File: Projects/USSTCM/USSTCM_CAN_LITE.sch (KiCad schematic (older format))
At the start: 1 part, among them U2 MCP25625

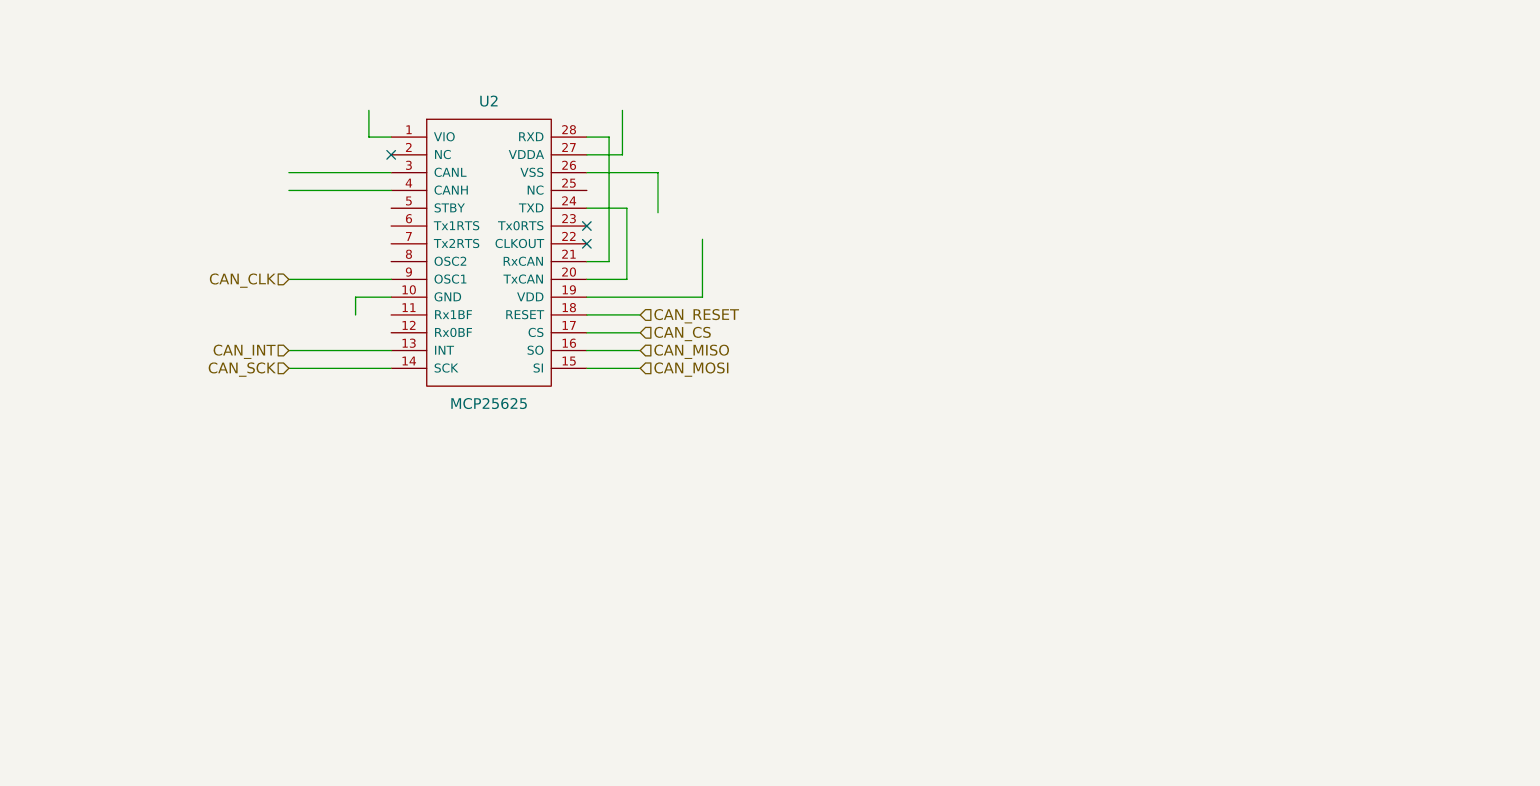
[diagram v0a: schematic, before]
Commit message: More organization of CMIO board
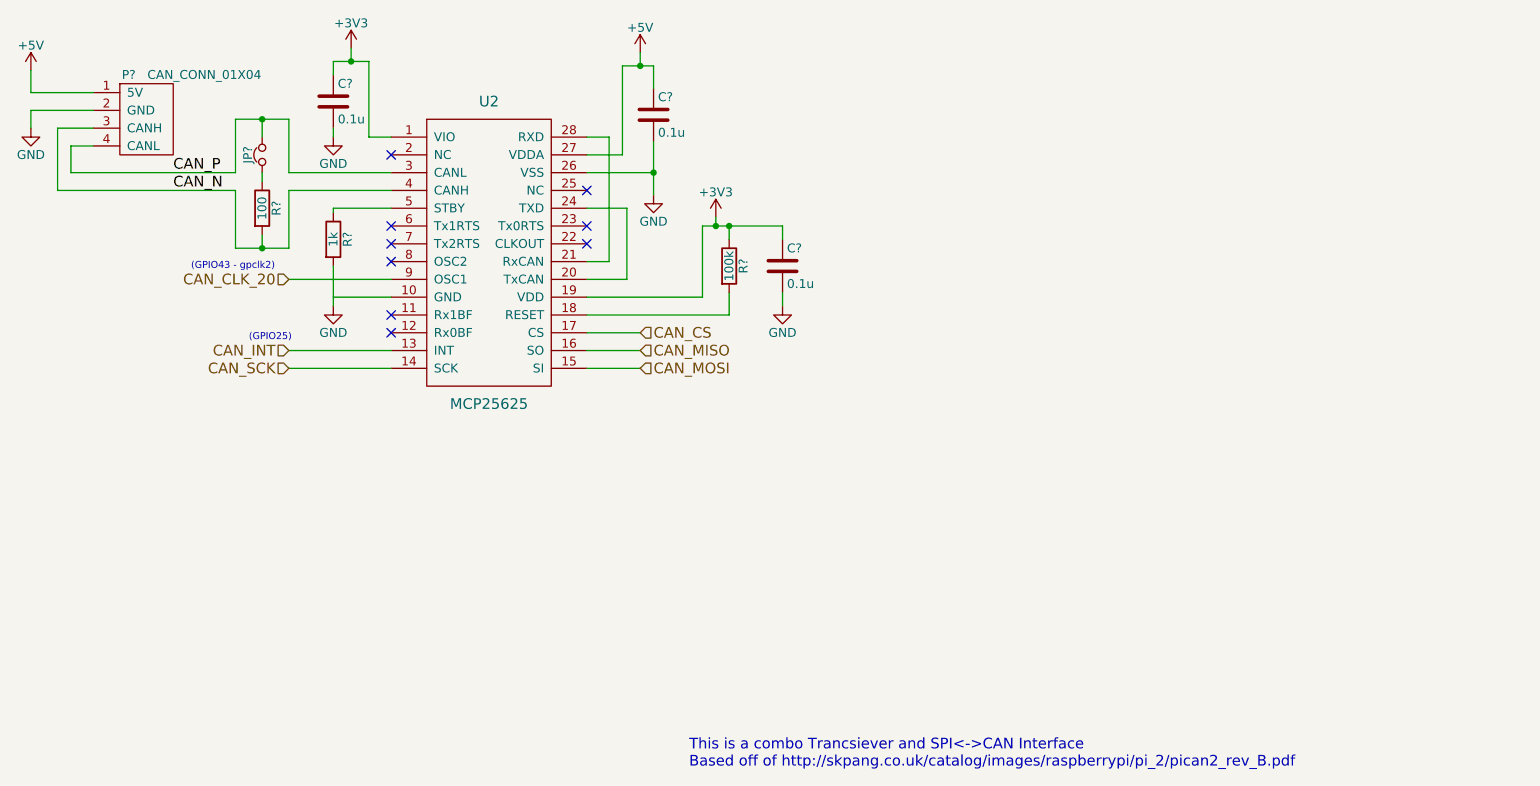
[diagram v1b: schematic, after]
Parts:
- added C? (x3): 0.1u, symbol C
- added JP?: Jumper_NC_Small, symbol Jumper_NC_Small
- added P?: CAN_CONN_01X04, symbol CAN_CONN_01X04
- added R?: 100, symbol R
- added R?: 100k, symbol R
- added R?: 1k, symbol R
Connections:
- net labels added: +3V3, +5V, CAN_CLK_20, CAN_N, CAN_P, GND
- net labels removed: CAN_CLK, CAN_RESET
- wire segments 25 -> 59
- no-connect marks 3 -> 9
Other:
- note added: "(GPIO25)"
- note added: "(GPIO43 - gpclk2)"
- note added: "This is a combo Trancsiever and SPI<->CAN Interface\nBased off of http://skpang.co.uk/catalog/images/raspberrypi/pi_2/pican2_rev_B.pdf"

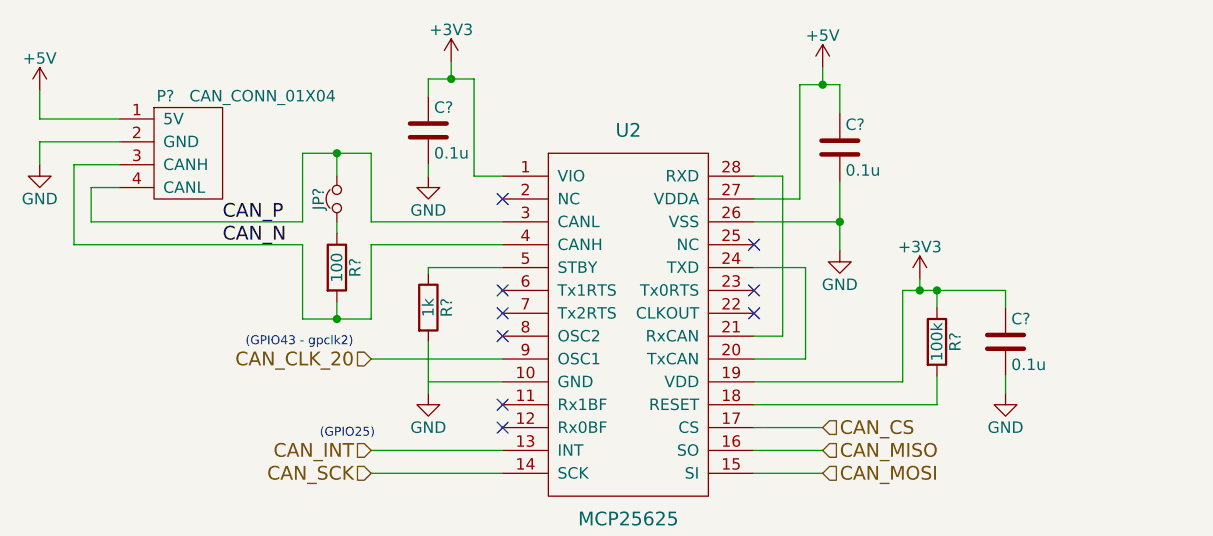
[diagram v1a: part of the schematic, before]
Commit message: added differential routes
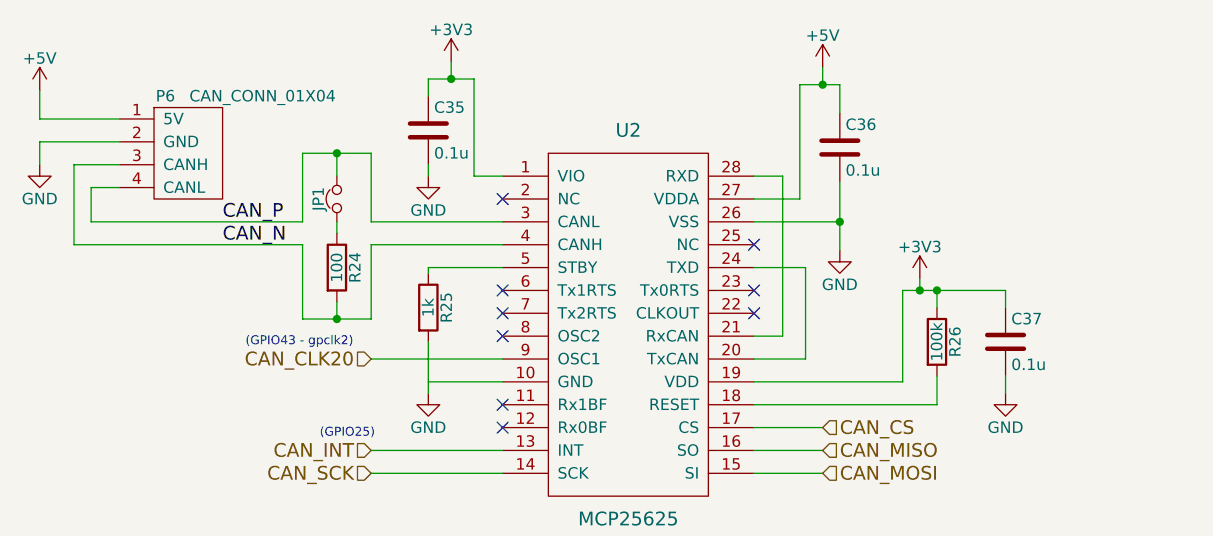
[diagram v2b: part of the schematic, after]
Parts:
- C35, C36, C37: renamed from C?; footprint (none) -> Capacitors_SMD:C_0805
- JP1: renamed from JP?; footprint (none) -> USST-footprints:J_0603
- P6: renamed from P?; footprint (none) -> Pin_Headers:Pin_Header_Angled_1x04_Pitch2.54mm
- R24, R25, R26: renamed from R?; footprint (none) -> Resistors_SMD:R_0805
- U2: footprint (none) -> Housings_SSOP:SSOP-28_5.3x10.2mm_Pitch0.65mm
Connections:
- net CAN_CLK_20 renamed CAN_CLK20
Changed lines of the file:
@@
 $Descr A4 11693 8268
 encoding utf-8
-Sheet 4 7
+Sheet 4 8
 Title ""
 Date ""
@@
 F 0 "U2" H 5825 4450 60  0000 C CNN
 F 1 "MCP25625" H 5825 2750 60  0000 C CNN
-F 2 "" H 5825 4000 60  0001 C CNN
+F 2 "Housings_SSOP:SSOP-28_5.3x10.2mm_Pitch0.65mm" H 5825 4000 60  0001 C CNN
 F 3 "" H 5825 4000 60  0001 C CNN
 	1    5825 3550
@@
 NoConn ~ 5275 2950
 Text HLabel 4700 3650 0    60   Input ~ 0
-CAN_CLK_20
+CAN_CLK20
 Text HLabel 4700 4050 0    60   Input ~ 0
 CAN_INT
@@
 NoConn ~ 6375 3450
 $Comp
-L GND #PWR?
+L GND #PWR076
 U 1 1 58E357D9
 P 4950 3800
-F 0 "#PWR?" H 4950 3550 50  0001 C CNN
+F 0 "#PWR076" H 4950 3550 50  0001 C CNN
 F 1 "GND" H 4950 3650 50  0000 C CNN
 F 2 "" H 4950 3800 50  0000 C CNN
@@
 (GPIO25)
 $Comp
-L R R?
+L R R24
 U 1 1 58E363A9
 P 4550 3250
-F 0 "R?" V 4630 3250 50  0000 C CNN
+F 0 "R24" V 4630 3250 50  0000 C CNN
 F 1 "100" V 4550 3250 50  0000 C CNN
-F 2 "" V 4480 3250 50  0000 C CNN
+F 2 "Resistors_SMD:R_0805" V 4480 3250 50  0001 C CNN
 F 3 "" H 4550 3250 50  0000 C CNN
 	1    4550 3250
@@
 $EndComp
 $Comp
-L Jumper_NC_Small JP?
+L Jumper_NC_Small JP1
 U 1 1 58E36400
 P 4550 2950
-F 0 "JP?" H 4550 3030 50  0000 C CNN
+F 0 "JP1" H 4550 3030 50  0000 C CNN
 F 1 "Jumper_NC_Small" H 4560 2890 50  0001 C CNN
-F 2 "" H 4550 2950 50  0000 C CNN
+F 2 "USST-footprints:J_0603" H 4550 2950 50  0001 C CNN
 F 3 "" H 4550 2950 50  0000 C CNN
 	1    4550 2950
@@
 $EndComp
 $Comp
-L CAN_CONN_01X04 P?
+L CAN_CONN_01X04 P6
 U 1 1 58E36E81
 P 3800 2750
-F 0 "P?" H 3800 3000 50  0000 C CNN
+F 0 "P6" H 3800 3000 50  0000 C CNN
 F 1 "CAN_CONN_01X04" H 4225 3000 50  0000 C CNN
-F 2 "" H 3800 2750 50  0000 C CNN
+F 2 "Pin_Headers:Pin_Header_Angled_1x04_Pitch2.54mm" H 3800 2750 50  0001 C CNN
 F 3 "" H 3800 2750 50  0000 C CNN
 	1    3800 2750
@@
 $EndComp
 $Comp
-L +5V #PWR?
+L +5V #PWR077
 U 1 1 58E38EE5
 P 3250 2475
-F 0 "#PWR?" H 3250 2325 50  0001 C CNN
+F 0 "#PWR077" H 3250 2325 50  0001 C CNN
 F 1 "+5V" H 3250 2615 50  0000 C CNN
 F 2 "" H 3250 2475 50  0000 C CNN
@@
 $EndComp
 $Comp
-L GND #PWR?
+L GND #PWR078
 U 1 1 58E38F41
 P 3250 2800
-F 0 "#PWR?" H 3250 2550 50  0001 C CNN
+F 0 "#PWR078" H 3250 2550 50  0001 C CNN
 F 1 "GND" H 3250 2650 50  0000 C CNN
 F 2 "" H 3250 2800 50  0000 C CNN
@@
 CAN_N
 $Comp
-L R R?
+L R R26
 U 1 1 58E3B222
 P 7175 3575
-F 0 "R?" V 7255 3575 50  0000 C CNN
+F 0 "R26" V 7255 3575 50  0000 C CNN
 F 1 "100k" V 7175 3575 50  0000 C CNN
-F 2 "" V 7105 3575 50  0000 C CNN
+F 2 "Resistors_SMD:R_0805" V 7105 3575 50  0001 C CNN
 F 3 "" H 7175 3575 50  0000 C CNN
 	1    7175 3575
@@
 $EndComp
 $Comp
-L +3V3 #PWR?
+L +3V3 #PWR079
 U 1 1 58E3B2CD
 P 7100 3300
-F 0 "#PWR?" H 7100 3150 50  0001 C CNN
+F 0 "#PWR079" H 7100 3150 50  0001 C CNN
 F 1 "+3V3" H 7100 3440 50  0000 C CNN
 F 2 "" H 7100 3300 50  0000 C CNN
@@
 $EndComp
 $Comp
-L C C?
+L C C37
 U 1 1 58E3BAA7
 P 7475 3575
-F 0 "C?" H 7500 3675 50  0000 L CNN
+F 0 "C37" H 7500 3675 50  0000 L CNN
 F 1 "0.1u" H 7500 3475 50  0000 L CNN
-F 2 "" H 7513 3425 50  0000 C CNN
+F 2 "Capacitors_SMD:C_0805" H 7513 3425 50  0001 C CNN
 F 3 "" H 7475 3575 50  0000 C CNN
 	1    7475 3575
@@
 $EndComp
 $Comp
-L GND #PWR?
+L GND #PWR080
 U 1 1 58E3BB18
 P 7475 3800
-F 0 "#PWR?" H 7475 3550 50  0001 C CNN
+F 0 "#PWR080" H 7475 3550 50  0001 C CNN
 F 1 "GND" H 7475 3650 50  0000 C CNN
 F 2 "" H 7475 3800 50  0000 C CNN
@@
 $EndComp
 $Comp
-L C C?
+L C C35
 U 1 1 58E3BBA6
 P 4950 2650
-F 0 "C?" H 4975 2750 50  0000 L CNN
+F 0 "C35" H 4975 2750 50  0000 L CNN
 F 1 "0.1u" H 4975 2550 50  0000 L CNN
-F 2 "" H 4988 2500 50  0000 C CNN
+F 2 "Capacitors_SMD:C_0805" H 4988 2500 50  0001 C CNN
 F 3 "" H 4950 2650 50  0000 C CNN
 	1    4950 2650
@@
 $EndComp
 $Comp
-L GND #PWR?
+L GND #PWR081
 U 1 1 58E3BC55
 P 4950 2850
-F 0 "#PWR?" H 4950 2600 50  0001 C CNN
+F 0 "#PWR081" H 4950 2600 50  0001 C CNN
 F 1 "GND" H 4950 2700 50  0000 C CNN
 F 2 "" H 4950 2850 50  0000 C CNN
@@
 $EndComp
 $Comp
-L +3V3 #PWR?
+L +3V3 #PWR082
 U 1 1 58E3BD05
 P 5050 2350
-F 0 "#PWR?" H 5050 2200 50  0001 C CNN
+F 0 "#PWR082" H 5050 2200 50  0001 C CNN
 F 1 "+3V3" H 5050 2490 50  0000 C CNN
 F 2 "" H 5050 2350 50  0000 C CNN
@@
 $EndComp
 $Comp
-L C C?
+L C C36
 U 1 1 58E3C137
 P 6750 2725
-F 0 "C?" H 6775 2825 50  0000 L CNN
+F 0 "C36" H 6775 2825 50  0000 L CNN
 F 1 "0.1u" H 6775 2625 50  0000 L CNN
-F 2 "" H 6788 2575 50  0000 C CNN
+F 2 "Capacitors_SMD:C_0805" H 6788 2575 50  0001 C CNN
 F 3 "" H 6750 2725 50  0000 C CNN
 	1    6750 2725
@@
 $EndComp
 $Comp
-L +5V #PWR?
+L +5V #PWR083
 U 1 1 58E3C2CD
 P 6675 2375
-F 0 "#PWR?" H 6675 2225 50  0001 C CNN
+F 0 "#PWR083" H 6675 2225 50  0001 C CNN
 F 1 "+5V" H 6675 2515 50  0000 C CNN
 F 2 "" H 6675 2375 50  0000 C CNN
@@
 $EndComp
 $Comp
-L GND #PWR?
+L GND #PWR084
 U 1 1 58E3CC67
 P 6750 3175
-F 0 "#PWR?" H 6750 2925 50  0001 C CNN
+F 0 "#PWR084" H 6750 2925 50  0001 C CNN
 F 1 "GND" H 6750 3025 50  0000 C CNN
 F 2 "" H 6750 3175 50  0000 C CNN
@@
 $EndComp
 $Comp
-L R R?
+L R R25
 U 1 1 58E3D50D
 P 4950 3425
-F 0 "R?" V 5030 3425 50  0000 C CNN
+F 0 "R25" V 5030 3425 50  0000 C CNN
 F 1 "1k" V 4950 3425 50  0000 C CNN
-F 2 "" V 4880 3425 50  0000 C CNN
+F 2 "Resistors_SMD:R_0805" V 4880 3425 50  0001 C CNN
 F 3 "" H 4950 3425 50  0000 C CNN
 	1    4950 3425
